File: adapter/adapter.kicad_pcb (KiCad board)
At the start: 2 copper layers, 91.8 x 23.6 mm, 10 parts, among them Q1 IRFB3004PbF, Q2 AUIRF2804S, U1 IRS10752LPbF, U2 P0102BL, U3 TLC555xD, U4 TLC555xP, U5 TLC555xP, U6 EL814, U7 TLC555xP

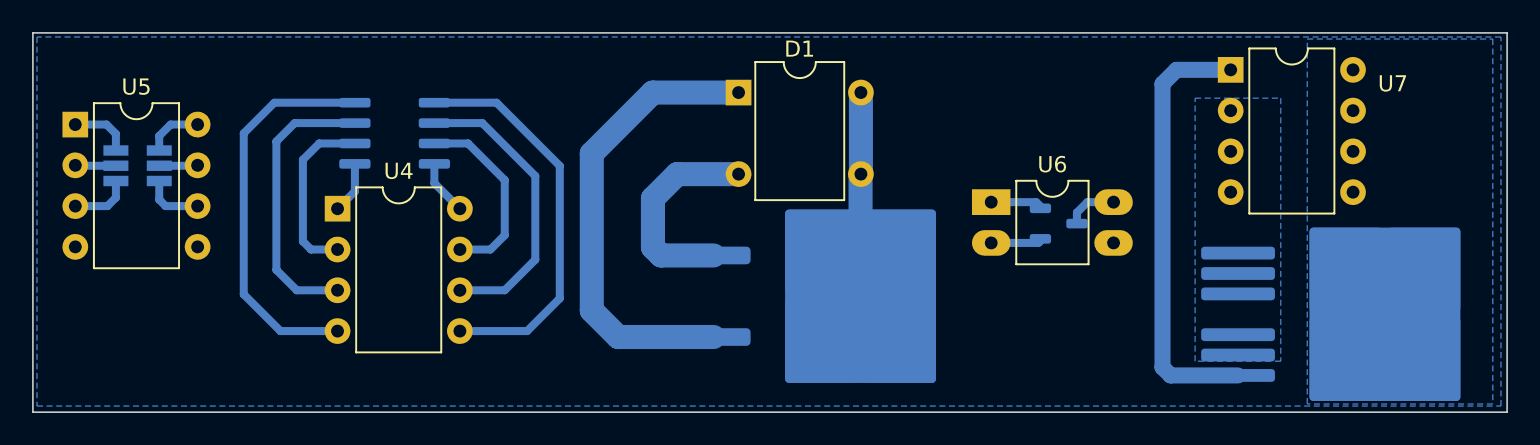
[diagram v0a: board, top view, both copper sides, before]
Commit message: [adapter] Update PCB
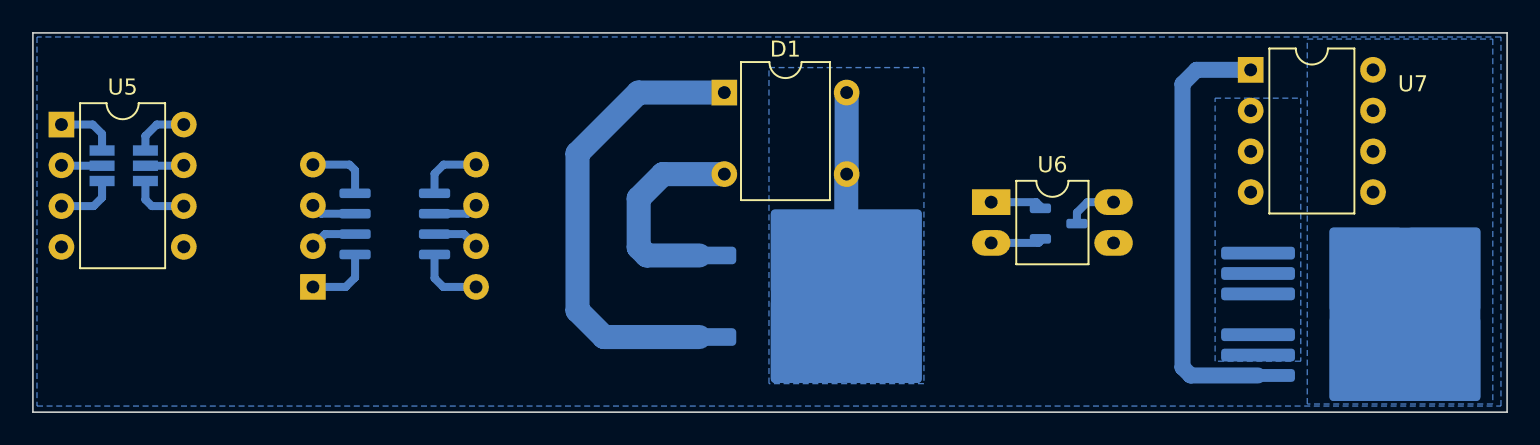
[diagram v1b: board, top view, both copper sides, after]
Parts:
- U4: footprint Package_DIP:DIP-8_W7.62mm -> Package_DIP:DIP-8_W10.16mm; moved to B.Cu
- moved U3 5.64 mm to (42.9, 27.9)
- moved U4 5.11 mm to (37.8, 31.8)
- moved U7 1.25 mm to (96.2, 18.3)
- moved Q2 1.25 mm to (104.3, 33.5)
- moved Q1 0.89 mm to (69.5, 32.4)
- moved D1 0.89 mm to (63.4, 19.7)
- moved U5 0.86 mm to (22.1, 21.7)
- moved U1 0.86 mm to (26.0, 24.3)
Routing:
- net /soic-8-5: track 24.8 -> 4.04 mm
- net /soic-8-4: track 24.5 -> 4.21 mm
- net /soic-8-6: track 18.4 -> 2.80 mm
- net /soic-8-3: track 17.7 -> 2.84 mm
- net /soic-8-7: track 11.9 -> 3.45 mm
- net /soic-8-2: track 11.1 -> 2.94 mm
- net /soic-8-1: track 3.24 -> 4.31 mm
- net /soic-8-8: track 3.45 -> 4.29 mm
- added copper zone on B.Cu, net /d2pak-2
